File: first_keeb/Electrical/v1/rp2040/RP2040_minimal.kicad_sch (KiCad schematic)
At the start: 65 parts, among them J1 Conn_01x04_Socket, P1 USB-TYPE-C-016, Q1 BSS138, SW1 TS-1187A-B-A-B, SW2 TS-1187A-B-A-B, SW3 BUTT1, SW4 BUTT3, SW5 BUTT2, U1 ME6208A44M3G, U2 ME6212C25M5G, U3 PRTR5V0U2X, U4 SLSS49E, U5 SLSS49E, U6 SLSS49E, U7 STM32F401RCTx, Y1 8MHz

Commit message: finishes rp2040 v1
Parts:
- removed C1: 4u7, Capacitor_SMD:C_0603_1608Metric, symbol Device:C_Small
- removed C11, C2, C3, C4, C5, C6: 100n, Capacitor_SMD:C_0402_1005Metric, symbol Device:C_Small
- removed C12, C13: 1u, Capacitor_SMD:C_0402_1005Metric, symbol Device:C_Small
- removed C14: 10n, Capacitor_SMD:C_0402_1005Metric, symbol Device:C_Small
- removed C20: 4u7, Capacitor_SMD:C_0805_2012Metric, symbol Device:C
- removed FB1: GZ2012D601TF, Capacitor_SMD:C_0805_2012Metric, symbol Device:FerriteBead
- removed R4, R5: 10k, Resistor_SMD:R_0402_1005Metric, symbol Device:R_Small
- removed U7: STM32F401RCTx, Package_QFP:LQFP-64_10x10mm_P0.5mm, symbol MCU_ST_STM32F4:STM32F401RCTx
- added C1, C11, C13, C2, C3, C4, C5, C6, C7, C8: 100n, Capacitor_SMD:C_0402_1005Metric, symbol Device:C
- added C10, C12, C9: 1u, Capacitor_SMD:C_0402_1005Metric, symbol Device:C
- added C18, C19: 10u, Capacitor_SMD:C_1206_3216Metric, symbol Device:C
- added R3, R4: 27R, Capacitor_SMD:C_0402_1005Metric, symbol Device:R
- added R5: 10k, Capacitor_SMD:C_0402_1005Metric, symbol Device:R
- added R6: 1k, Capacitor_SMD:C_0402_1005Metric, symbol Device:R
- added U3: RP2040, MCU_RaspberryPi_and_Boards:RP2040-QFN-56, symbol MCU_RaspberryPi_RP2040:RP2040
- added U5: W25Q16JVSS, Package_SO:SOIC-8_5.23x5.23mm_P1.27mm, symbol Memory_Flash:W25Q32JVSS
- added U6: ME6212C33M5G, Package_TO_SOT_SMD:SOT-23-5, symbol Regulator_Linear:AP2127K-3.3
- renumbered C7 to C14, C8 to C15, C9 to C16, C10 to C17, C18 to C20, C19 to C21, C15 to C22, C16 to C23, C17 to C24, C21 to C25, C22 to C26, C23 to C27, C24 to C28, C25 to C29, C26 to C30, C27 to C31, C28 to C32, C29 to C33, C30 to C34, R3 to R7, R6 to R8, R7 to R9, U3 to U1, U1 to U2, U2 to U4, U6 to U7, U4 to U8, U5 to U9
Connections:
- net BOOT0 is gone; now on net GND: SW1.1
- net NRST is gone; now on net GND: SW2.1
- net +5V: now also C18.1, U6.1 (VIN), U6.3 (EN)
- net ADC_IN1: now also U3.38 (GPIO26_ADC0)
- net ADC_IN2: now also U3.39 (GPIO27_ADC1)
- net ADC_IN3: now also U3.41 (GPIO29_ADC3)
- net BUTT0: now also U3.28 (GPIO17)
- net BUTT1: now also U3.29 (GPIO18)
- net BUTT2: now also U3.30 (GPIO19)
- net GND: now also C1.2, C10.2, C11.2, C12.2, C13.2, C18.2, C19.2, C2.2, C3.2, C4.2, C5.2, C6.2, C7.2, C8.2, C9.2, U3.19 (TESTEN), U3.57 (GND), U5.4 (GND), U6.2 (GND); no longer SW2.2
- net LED_D: now also U3.15 (GPIO12)
- net OSC_IN: now also U3.20 (XIN)
- net OSC_OUT: now also U3.21 (XOUT)
- net SWCLK: now also J1.2 (Pin_2), U3.24 (SWCLK); no longer J1.3 (Pin_3)
- net SWDIO: now also J1.3 (Pin_3), U3.25 (SWD); no longer J1.2 (Pin_2)
- net USB_D+: now also R3.1
- net USB_D-: now also R4.1
- net VDD renamed +3V3
- net +3V3: now also C10.1, C13.1, C19.1, C3.1, C4.1, C5.1, C6.1, C7.1, C8.1, R5.1, U3.1 (IOVDD), U3.10 (IOVDD), U3.22 (IOVDD), U3.33 (IOVDD), U3.42 (IOVDD), U3.44 (VREG_IN), U3.48 (USB_VDD), U3.49 (IOVDD), U5.8 (VCC), U6.5 (VOUT); no longer C17.1, SW1.2, U4.5 (VOUT)
- new net: SW2.2, U3.26 (RUN)
- new net: R4.2, U3.46 (USB_DM)
- new net: R3.2, U3.47 (USB_DP)
- new net: R6.1, SW1.2
- new net +1V1: C1.1, C2.1, C9.1, U3.23 (DVDD), U3.45 (VREG_VOUT), U3.50 (DVDD)
- new net ADC_AVDD: C11.1, C12.1, C17.1, U3.43 (ADC_AVDD), U4.5 (VOUT)
- new net GPIO0: U3.2 (GPIO0)
- new net GPIO1: U3.3 (GPIO1)
- new net GPIO10: U3.13 (GPIO10)
- new net GPIO11: U3.14 (GPIO11)
- new net GPIO13: U3.16 (GPIO13)
- new net GPIO14: U3.17 (GPIO14)
- new net GPIO15: U3.18 (GPIO15)
- new net GPIO16: U3.27 (GPIO16)
- new net GPIO2: U3.4 (GPIO2)
- new net GPIO20: U3.31 (GPIO20)
- new net GPIO21: U3.32 (GPIO21)
- new net GPIO22: U3.34 (GPIO22)
- new net GPIO23: U3.35 (GPIO23)
- new net GPIO24: U3.36 (GPIO24)
- new net GPIO25: U3.37 (GPIO25)
- new net GPIO28_ADC2: U3.40 (GPIO28_ADC2)
- new net GPIO3: U3.5 (GPIO3)
- new net GPIO4: U3.6 (GPIO4)
- new net GPIO5: U3.7 (GPIO5)
- new net GPIO6: U3.8 (GPIO6)
- new net GPIO7: U3.9 (GPIO7)
- new net GPIO8: U3.11 (GPIO8)
- new net GPIO9: U3.12 (GPIO9)
- new net QSPI_SCLK: U3.52 (QSPI_SCLK), U5.6 (CLK)
- new net QSPI_SD0: U3.53 (QSPI_SD0), U5.5 (DI(IO0))
- new net QSPI_SD1: U3.55 (QSPI_SD1), U5.2 (DO(IO1))
- new net QSPI_SD2: U3.54 (QSPI_SD2), U5.3 (IO2)
- new net QSPI_SD3: U3.51 (QSPI_SD3), U5.7 (IO3)
- new net QSPI_SS: R5.2, R6.2, U3.56 (QSPI_SS), U5.1 (~{CS})
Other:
- note added: "50mW"
- note added: "ADC VREF"
- note added: "All Capacitors 6.3V, XR5, 10%"
- note added: "All resistors 1%"
- note added: "Ensure 100n is close to pin 43 (ADC_AVDD)"
- note added: "Flash"
- note added: "Make sure 1u C is close to pin 45 of RP2040"
- note added: "Make sure R3 and R4 are close to RP2040"
- note added: "Make sure is close to pin 44 of RP2040"
- note added: "RP2040"
- note added: "RP2040 Breakout"
- moved on the sheet: C14, C15, C16, C17, C20, C21, C22, C23, C24, C25, C26, C27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

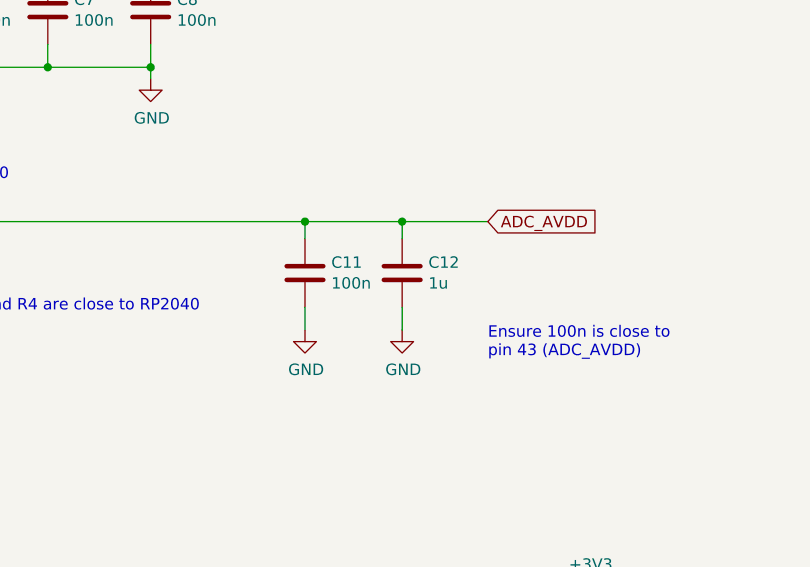
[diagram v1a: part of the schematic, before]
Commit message: adds 10n and 100n capactiros near rp2040 adc_avdd
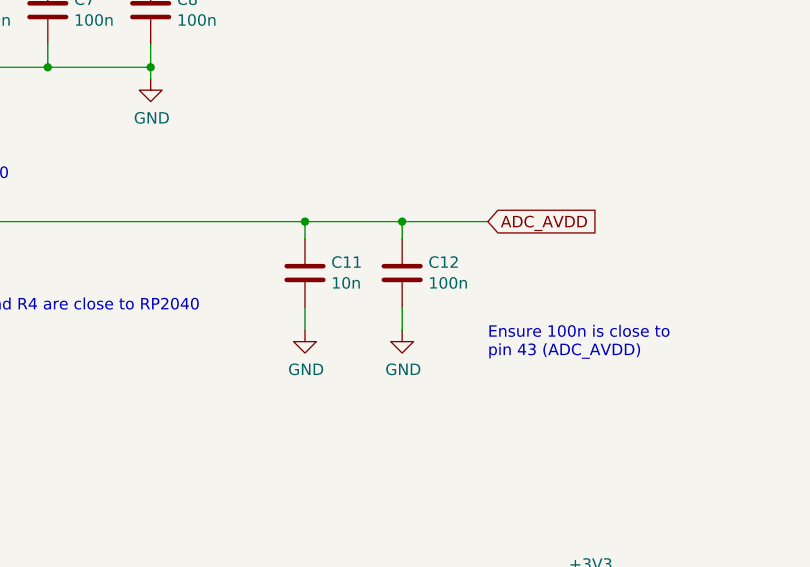
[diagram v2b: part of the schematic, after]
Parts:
- C11: value 100n -> 10n
- C12: value 1u -> 100n
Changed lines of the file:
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@@
       (effects (font (size 1.27 1.27)) (justify left))
     )
-    (property "Value" "100n" (at 202.311 66.548 0)
+    (property "Value" "10n" (at 202.311 66.548 0)
       (effects (font (size 1.27 1.27)) (justify left))
     )
@@
       (effects (font (size 1.27 1.27)) (justify left))
     )
-    (property "Value" "1u" (at 213.106 66.548 0)
-      (effects (font (size 1.27 1.27)) (justify left))
-    )
+    (property "Value" "100n" (at 213.106 66.548 0)
+      (effects (font (size 1.27 1.27)) (justify left))
+    )

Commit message: puts 10n and 1u caps to decouple adv_avdd on rp2040 to match the stm32 adc vref
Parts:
- C12: value 100n -> 1u
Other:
- note added: "1u C close to pin 45 of RP2040"
- note added: "1u close to pin 44 of RP2040"
- note removed: "Make sure 1u C is close to pin 45 of RP2040"
- note removed: "Make sure R3 and R4 are close to RP2040"
- note removed: "Make sure is close to pin 44 of RP2040"
- moved on the sheet: C11, C12
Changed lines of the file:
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@@
   (junction (at 112.395 51.435) (diameter 0) (color 0 0 0 0)
   )
-  (junction (at 199.39 59.69) (diameter 0) (color 0 0 0 0)
+  (junction (at 176.53 59.69) (diameter 0) (color 0 0 0 0)
   )
   (junction (at 125.095 31.115) (diameter 0) (color 0 0 0 0)
@@
   (junction (at 170.815 31.115) (diameter 0) (color 0 0 0 0)
   )
-  (junction (at 210.185 59.69) (diameter 0) (color 0 0 0 0)
+  (junction (at 187.325 59.69) (diameter 0) (color 0 0 0 0)
   )
   (junction (at 231.14 104.775) (diameter 0) (color 0 0 0 0)
@@
     (stroke (width 0) (type default))
   )
-  (wire (pts (xy 210.185 59.69) (xy 210.185 61.595))
+  (wire (pts (xy 187.325 59.69) (xy 187.325 61.595))
     (stroke (width 0) (type default))
   )
@@
     (stroke (width 0) (type default))
   )
-  (wire (pts (xy 199.39 59.69) (xy 210.185 59.69))
+  (wire (pts (xy 176.53 59.69) (xy 187.325 59.69))
     (stroke (width 0) (type default))
   )
@@
     (stroke (width 0) (type default))
   )
-  (wire (pts (xy 199.39 69.215) (xy 199.39 71.755))
+  (wire (pts (xy 176.53 69.215) (xy 176.53 71.755))
     (stroke (width 0) (type default))
   )
@@
     (stroke (width 0) (type default))
   )
-  (wire (pts (xy 137.795 59.69) (xy 199.39 59.69))
+  (wire (pts (xy 137.795 59.69) (xy 176.53 59.69))
     (stroke (width 0) (type default))
   )
@@
     (stroke (width 0) (type default))
   )
-  (wire (pts (xy 210.185 69.215) (xy 210.185 71.755))
+  (wire (pts (xy 187.325 69.215) (xy 187.325 71.755))
     (stroke (width 0) (type default))
   )
@@
     (stroke (width 0) (type default))
   )
-  (wire (pts (xy 199.39 59.69) (xy 199.39 61.595))
+  (wire (pts (xy 176.53 59.69) (xy 176.53 61.595))
     (stroke (width 0) (type default))
   )
@@
     (stroke (width 0) (type default))
   )
-  (wire (pts (xy 210.185 59.69) (xy 219.71 59.69))
+  (wire (pts (xy 187.325 59.69) (xy 196.85 59.69))
     (stroke (width 0) (type default))
   )
@@
     (effects (font (size 2.54 2.54)) (justify left bottom))
   )
-  (text "Ensure 100n is close to \npin 43 (ADC_AVDD)" (at 219.71 74.93 0)
+  (text "Ensure 100n is close to \npin 43 (ADC_AVDD)" (at 193.04 74.295 0)
     (effects (font (size 1.27 1.27)) (justify left bottom))
   )
-  (text "Make sure is close to pin 44 of RP2040" (at 132.715 55.245 0)
+  (text "1u close to \npin 44 of RP2040" (at 133.35 54.61 0)
     (effects (font (size 1.27 1.27)) (justify left bottom))
   )
-  (text "Make sure 1u C is close to \npin 45 of RP2040" (at 40.64 55.88 0)
+  (text "1u C close to \npin 45 of RP2040" (at 46.99 54.61 0)
     (effects (font (size 1.27 1.27)) (justify left bottom))
   )
@@
     (effects (font (size 2.54 2.54)) (justify left bottom))
   )
-  (text "Make sure R3 and R4 are close to RP2040" (at 151.13 69.85 0)
-    (effects (font (size 1.27 1.27)) (justify left bottom))
-  )
   (text "Cleft = Cright = 2 * (CL - Cstray)\n\nCstray assumed to be 5pf"
     (at 182.88 195.58 0)
@@
     (effects (font (size 1.27 1.27)) (justify right bottom))
   )
-  (global_label "ADC_AVDD" (shape input) (at 219.71 59.69 0) (fields_autoplaced)
+  (global_label "ADC_AVDD" (shape input) (at 196.85 59.69 0) (fields_autoplaced)
     (effects (font (size 1.27 1.27)) (justify left))
-    (property "Intersheetrefs" "${INTERSHEET_REFS}" (at 231.275 59.69 0)
+    (property "Intersheetrefs" "${INTERSHEET_REFS}" (at 208.415 59.69 0)
       (effects (font (size 1.27 1.27)) (justify left) hide)
     )
@@
     )
   )
-  (symbol (lib_id "power:GND") (at 210.185 71.755 0) (unit 1)
+  (symbol (lib_id "power:GND") (at 187.325 71.755 0) (unit 1)
     (in_bom yes) (on_board yes) (dnp no)
-    (property "Reference" "#PWR013" (at 210.185 78.105 0)
+    (property "Reference" "#PWR013" (at 187.325 78.105 0)
       (effects (font (size 1.27 1.27)) hide)
     )
-    (property "Value" "GND" (at 210.312 76.1492 0)
+    (property "Value" "GND" (at 187.452 76.1492 0)
       (effects (font (size 1.27 1.27)))
     )
-    (property "Footprint" "" (at 210.185 71.755 0)
+    (property "Footprint" "" (at 187.325 71.755 0)
       (effects (font (size 1.27 1.27)) hide)
     )
-    (property "Datasheet" "" (at 210.185 71.755 0)
+    (property "Datasheet" "" (at 187.325 71.755 0)
       (effects (font (size 1.27 1.27)) hide)
     )
@@
     )
   )
-  (symbol (lib_id "power:GND") (at 199.39 71.755 0) (unit 1)
+  (symbol (lib_id "power:GND") (at 176.53 71.755 0) (unit 1)
     (in_bom yes) (on_board yes) (dnp no)
-    (property "Reference" "#PWR012" (at 199.39 78.105 0)
+    (property "Reference" "#PWR012" (at 176.53 78.105 0)
       (effects (font (size 1.27 1.27)) hide)
     )
-    (property "Value" "GND" (at 199.517 76.1492 0)
+    (property "Value" "GND" (at 176.657 76.1492 0)
       (effects (font (size 1.27 1.27)))
     )
-    (property "Footprint" "" (at 199.39 71.755 0)
+    (property "Footprint" "" (at 176.53 71.755 0)
       (effects (font (size 1.27 1.27)) hide)
     )
-    (property "Datasheet" "" (at 199.39 71.755 0)
+    (property "Datasheet" "" (at 176.53 71.755 0)
       (effects (font (size 1.27 1.27)) hide)
     )
@@
     )
   )
-  (symbol (lib_id "Device:C") (at 199.39 65.405 0) (unit 1)
+  (symbol (lib_id "Device:C") (at 176.53 65.405 0) (unit 1)
     (in_bom yes) (on_board yes) (dnp no)
-    (property "Reference" "C11" (at 202.311 64.2366 0)
+    (property "Reference" "C11" (at 179.451 64.2366 0)
       (effects (font (size 1.27 1.27)) (justify left))
     )
-    (property "Value" "10n" (at 202.311 66.548 0)
+    (property "Value" "10n" (at 179.451 66.548 0)
       (effects (font (size 1.27 1.27)) (justify left))
     )
-    (property "Footprint" "Capacitor_SMD:C_0402_1005Metric" (at 200.3552 69.215 0)
+    (property "Footprint" "Capacitor_SMD:C_0402_1005Metric" (at 177.4952 69.215 0)
       (effects (font (size 1.27 1.27)) hide)
     )
-    (property "Datasheet" "~" (at 199.39 65.405 0)
+    (property "Datasheet" "~" (at 176.53 65.405 0)
       (effects (font (size 1.27 1.27)) hide)
     )
@@
     )
   )
-  (symbol (lib_id "Device:C") (at 210.185 65.405 0) (unit 1)
+  (symbol (lib_id "Device:C") (at 187.325 65.405 0) (unit 1)
     (in_bom yes) (on_board yes) (dnp no)
-    (property "Reference" "C12" (at 213.106 64.2366 0)
+    (property "Reference" "C12" (at 190.246 64.2366 0)
       (effects (font (size 1.27 1.27)) (justify left))
     )
-    (property "Value" "100n" (at 213.106 66.548 0)
+    (property "Value" "1u" (at 190.246 66.548 0)
       (effects (font (size 1.27 1.27)) (justify left))
     )
-    (property "Footprint" "Capacitor_SMD:C_0402_1005Metric" (at 211.1502 69.215 0)
+    (property "Footprint" "Capacitor_SMD:C_0402_1005Metric" (at 188.2902 69.215 0)
       (effects (font (size 1.27 1.27)) hide)
     )
-    (property "Datasheet" "~" (at 210.185 65.405 0)
+    (property "Datasheet" "~" (at 187.325 65.405 0)
       (effects (font (size 1.27 1.27)) hide)
     )

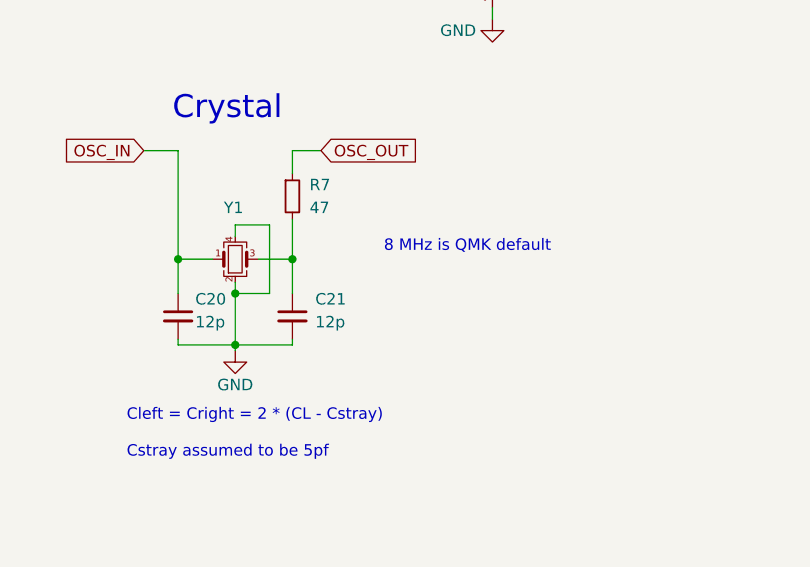
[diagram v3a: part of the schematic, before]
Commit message: moves plates together
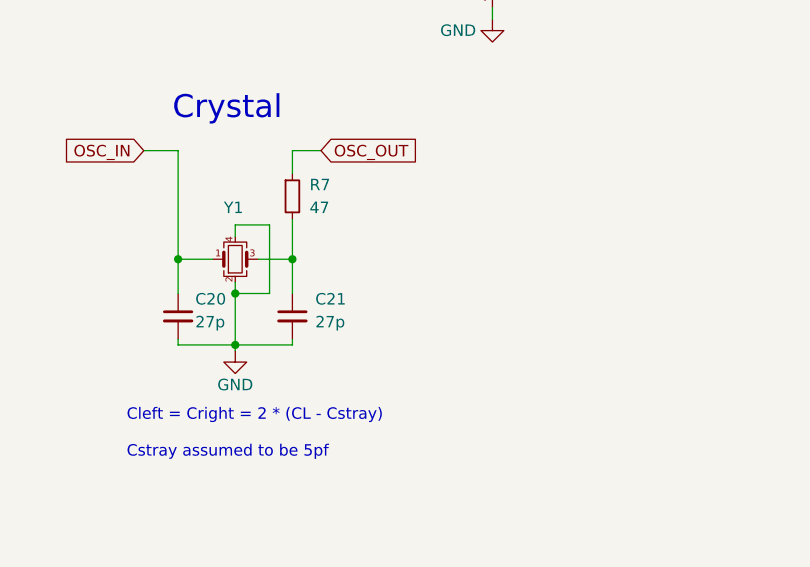
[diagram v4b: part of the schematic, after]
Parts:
- C20, C21: value 12p -> 27p; LCSC Part # C1547 -> (none)
- Y1: value 8MHz -> 12MHz; LCSC Part # C13738 -> C9002
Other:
- note removed: "8 MHz is QMK default"
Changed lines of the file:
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@@
     (effects (font (size 1.27 1.27)) (justify left bottom))
   )
-  (text "8 MHz is QMK default" (at 211.455 172.72 0)
-    (effects (font (size 1.27 1.27)) (justify left bottom))
-  )
   (text "Backlights" (at 78.105 247.015 0)
     (effects (font (size 2.54 2.54)) (justify left bottom))
@@
       (effects (font (size 1.27 1.27)) (justify left))
     )
-    (property "Value" "8MHz" (at 191.77 167.64 0)
+    (property "Value" "12MHz" (at 191.77 167.64 0)
       (effects (font (size 1.27 1.27)) (justify left) hide)
     )
@@
       (effects (font (size 1.27 1.27)) hide)
     )
-    (property "Datasheet" "~" (at 194.945 173.355 0)
+    (property "Datasheet" "X322512MSB4SI" (at 194.945 173.355 0)
       (effects (font (size 1.27 1.27)) hide)
     )
-    (property "LCSC Part #" "C13738" (at 194.945 173.355 0)
+    (property "LCSC Part #" "C9002" (at 194.945 173.355 0)
       (effects (font (size 1.27 1.27)) hide)
     )
@@
       (effects (font (size 1.27 1.27)) (justify left))
     )
-    (property "Value" "12p" (at 190.5 180.34 0)
+    (property "Value" "27p" (at 190.5 180.34 0)
       (effects (font (size 1.27 1.27)) (justify left))
     )
@@
       (effects (font (size 1.27 1.27)) hide)
     )
-    (property "LCSC Part #" "C1547" (at 188.595 179.705 0)
+    (property "LCSC Part #" "" (at 188.595 179.705 0)
       (effects (font (size 1.27 1.27)) hide)
     )
@@
       (effects (font (size 1.27 1.27)) (justify left))
     )
-    (property "Value" "12p" (at 203.835 180.34 0)
+    (property "Value" "27p" (at 203.835 180.34 0)
       (effects (font (size 1.27 1.27)) (justify left))
     )
@@
       (effects (font (size 1.27 1.27)) hide)
     )
-    (property "LCSC Part #" "C1547" (at 201.295 179.705 0)
+    (property "LCSC Part #" "" (at 201.295 179.705 0)
       (effects (font (size 1.27 1.27)) hide)
     )
